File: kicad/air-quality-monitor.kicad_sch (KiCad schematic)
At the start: 28 parts, among them J1 USB-C power only, J2 SCD40 breakout, J3 OLED SSD1306, J4 SPS30, J5 Qwiic, J6 Qwiic, U1 AP2112K-3.3, U2 AP2112K-3.3, U3 ESP32-C6-DevKitC-1

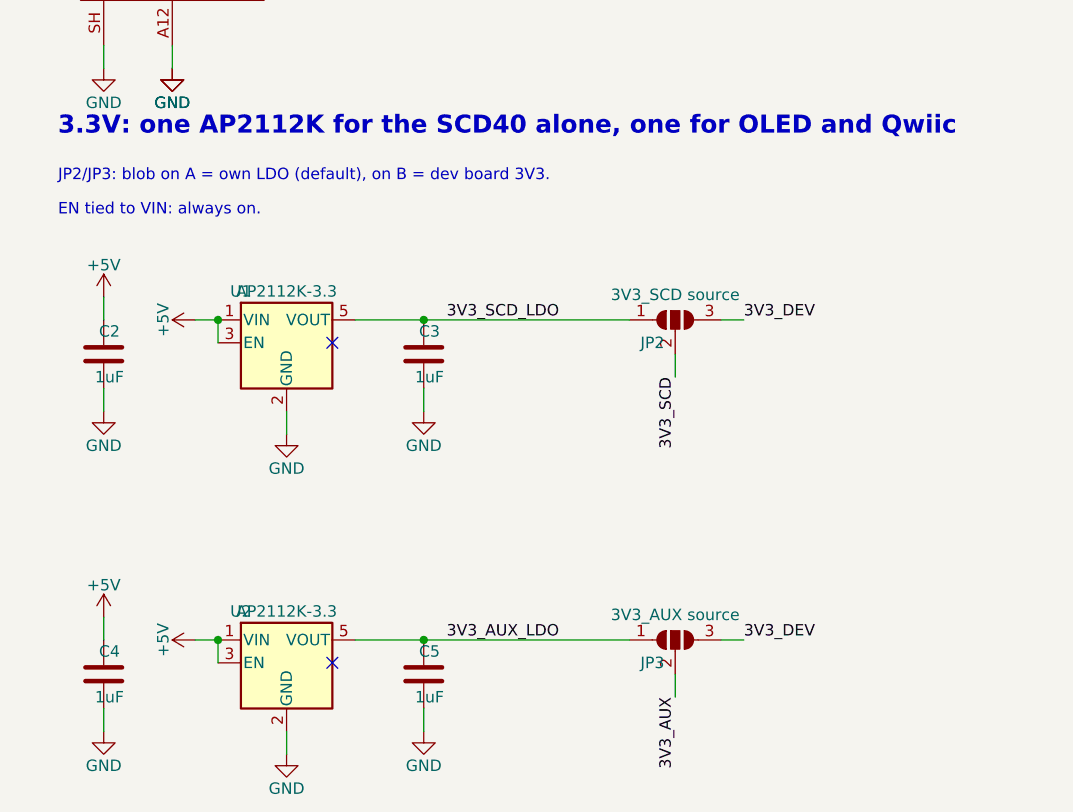
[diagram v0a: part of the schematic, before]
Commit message: Bridge both 3.3V jumpers to their LDO from the factory
With open jumpers the 3.3V rails were dead until a blob was soldered.
Now the board works as delivered, and switching a rail to the dev
board's 3V3 means cutting the trace and adding a blob.

Co-Authored-By: Claude Opus 5.5 <noreply@anthropic.com>
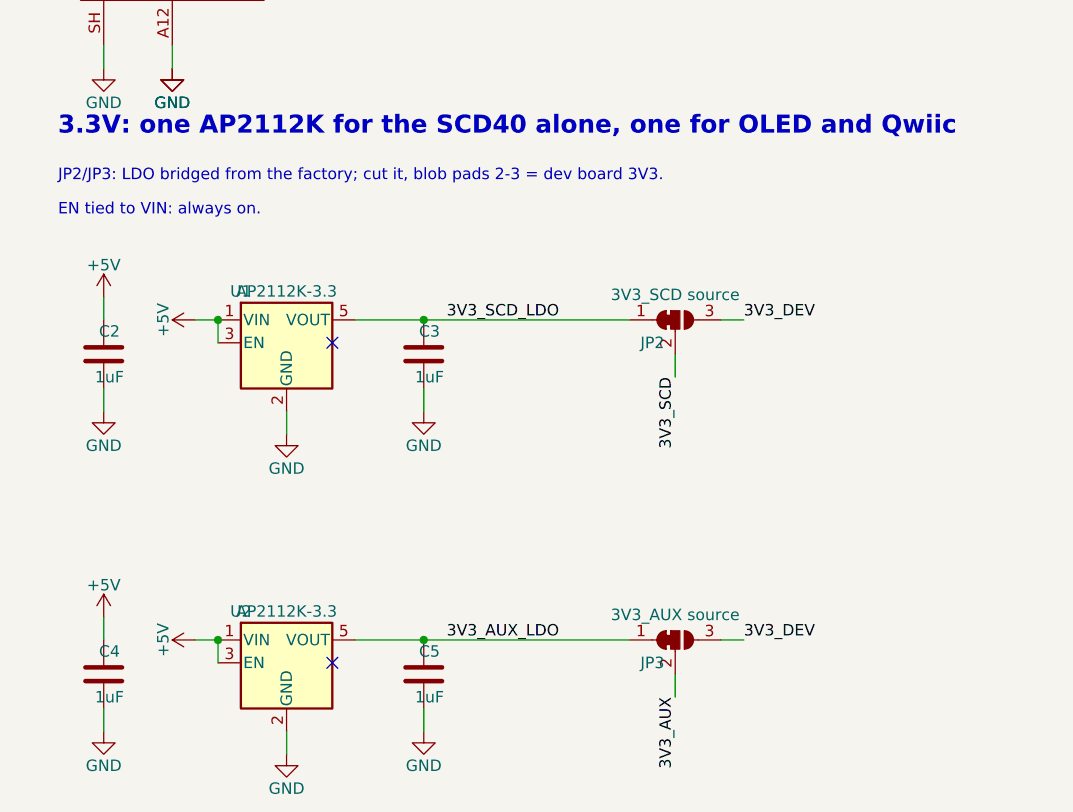
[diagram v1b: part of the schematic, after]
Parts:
- JP2, JP3: footprint Jumper:SolderJumper-3_P1.3mm_Open_RoundedPad1.0x1.5mm_NumberLabels -> Jumper:SolderJumper-3_P1.3mm_Bridged12_RoundedPad1.0x1.5mm_NumberLabels; symbol Jumper:SolderJumper_3_Open -> Jumper:SolderJumper_3_Bridged12
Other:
- note added: "JP2/JP3: LDO bridged from the factory; cut it, blob pads 2-3 = dev board 3V3."
- note removed: "JP2/JP3: blob on A = own LDO (default), on B = dev board 3V3."
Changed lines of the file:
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@@
 		)
 	)
-	(text "JP2/JP3: blob on A = own LDO (default), on B = dev board 3V3."
+	(text "JP2/JP3: LDO bridged from the factory; cut it, blob pads 2-3 = dev board 3V3."
 		(exclude_from_sim no)
 		(at 25.4 99.06 0)
@@
 	)
 	(symbol
-		(lib_id "Jumper:SolderJumper_3_Open")
+		(lib_id "Jumper:SolderJumper_3_Bridged12")
 		(at 93.98 149.86 0)
 		(unit 1)
@@
 			)
 		)
-		(property "Footprint" "Jumper:SolderJumper-3_P1.3mm_Open_RoundedPad1.0x1.5mm_NumberLabels"
+		(property "Footprint" "Jumper:SolderJumper-3_P1.3mm_Bridged12_RoundedPad1.0x1.5mm_NumberLabels"
 			(at 93.98 149.86 0)
 			(hide yes)
@@
 	)
 	(symbol
-		(lib_id "Jumper:SolderJumper_3_Open")
+		(lib_id "Jumper:SolderJumper_3_Bridged12")
 		(at 93.98 114.3 0)
 		(unit 1)
@@
 			)
 		)
-		(property "Footprint" "Jumper:SolderJumper-3_P1.3mm_Open_RoundedPad1.0x1.5mm_NumberLabels"
+		(property "Footprint" "Jumper:SolderJumper-3_P1.3mm_Bridged12_RoundedPad1.0x1.5mm_NumberLabels"
 			(at 93.98 114.3 0)
 			(hide yes)

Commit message: Use a jumper cap across D1 so the dev board gets the full 5V
Behind the Schottky the dev board's 5V pin sees about 4.6V, less than
the 4.9V that already sent an ESP32-S3 board with the same AMS1117
into a brownout loop. A cap fails safe: a loose one only puts the
diode back in the path. It comes off only when both USB cables are in.

Co-Authored-By: Claude Opus 5.5 <noreply@anthropic.com>
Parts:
- JP1: footprint Jumper:SolderJumper-2_P1.3mm_Open_RoundedPad1.0x1.5mm -> Connector_PinHeader_2.54mm:PinHeader_1x02_P2.54mm_Vertical; symbol Jumper:SolderJumper_2_Open -> Jumper:Jumper_2_Bridged
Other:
- note added: "JP1 cap on (default) bypasses D1: full 5V for the dev board. Pull it before plugging in both."
- note removed: "JP1 bridges the diode: dev board USB powers the PCB. Then never plug in both."
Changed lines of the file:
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@@
 		)
 	)
-	(text "JP1 bridges the diode: dev board USB powers the PCB. Then never plug in both."
+	(text "JP1 cap on (default) bypasses D1: full 5V for the dev board. Pull it before plugging in both."
 		(exclude_from_sim no)
 		(at 137.16 41.91 0)
@@
 	)
 	(symbol
-		(lib_id "Jumper:SolderJumper_2_Open")
+		(lib_id "Jumper:Jumper_2_Bridged")
 		(at 157.48 66.04 0)
 		(unit 1)
@@
 			)
 		)
-		(property "Footprint" "Jumper:SolderJumper-2_P1.3mm_Open_RoundedPad1.0x1.5mm"
+		(property "Footprint" "Connector_PinHeader_2.54mm:PinHeader_1x02_P2.54mm_Vertical"
 			(at 157.48 66.04 0)
 			(hide yes)

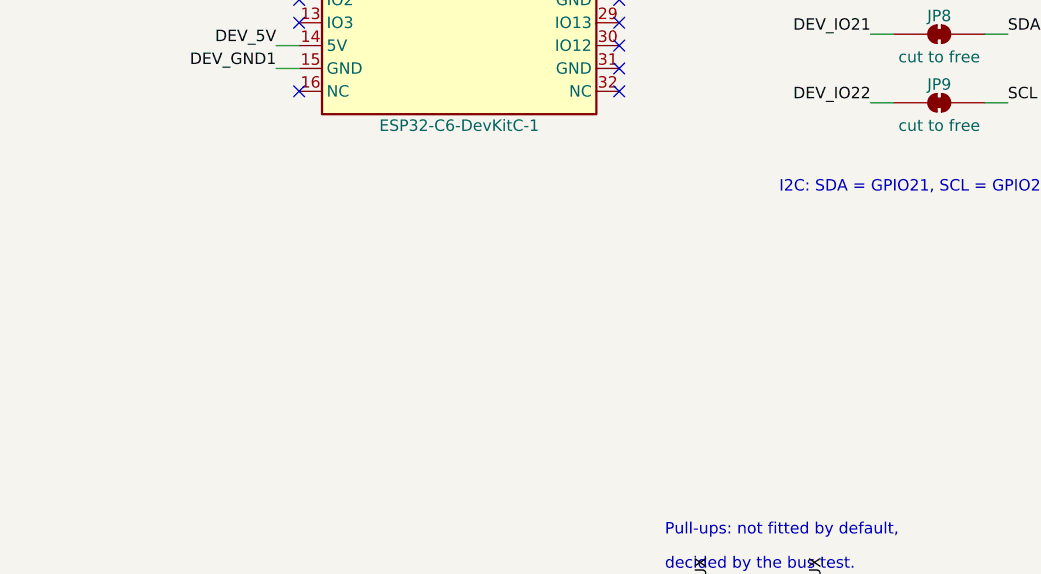
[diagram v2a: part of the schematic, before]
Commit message: Leave room for bulk capacitors on the dev board's 3V3
The same S3 board that browned out at 5.0V booted once 100+470µF sat
on its 3V3 pin. Two optional footprints there keep that fix one
solder job away, without fitting it on boards that don't need it.

Co-Authored-By: Claude Opus 5.5 <noreply@anthropic.com>
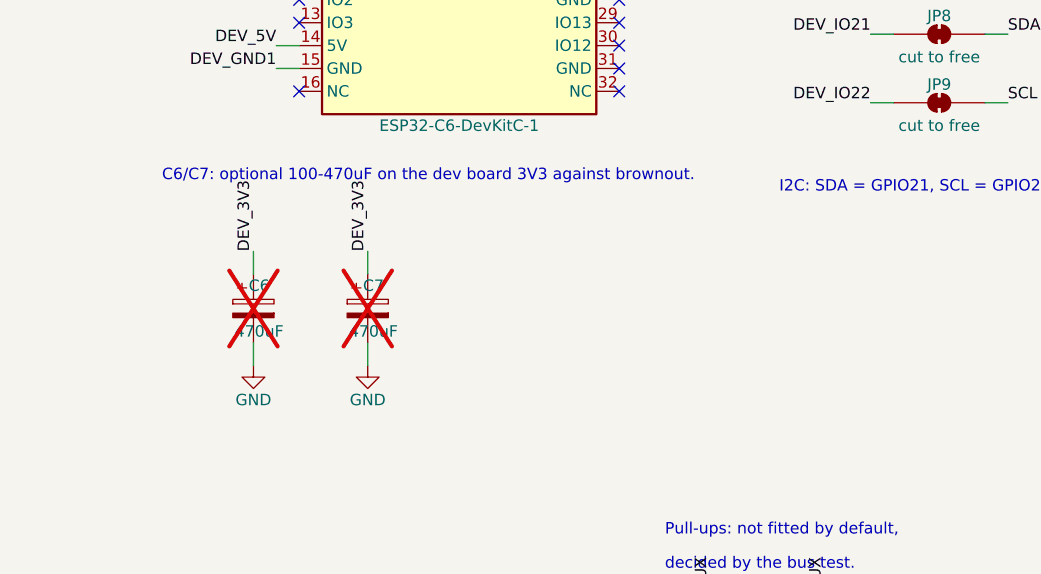
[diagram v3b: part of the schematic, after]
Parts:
- added C6, C7: 470uF, Capacitor_THT:CP_Radial_D8.0mm_P2.50mm, symbol Device:C_Polarized
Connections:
- net DEV_3V3: now also C6.1, C7.1
- net GND: now also C6.2, C7.2
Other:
- note added: "C6/C7: optional 100-470uF on the dev board 3V3 against brownout."

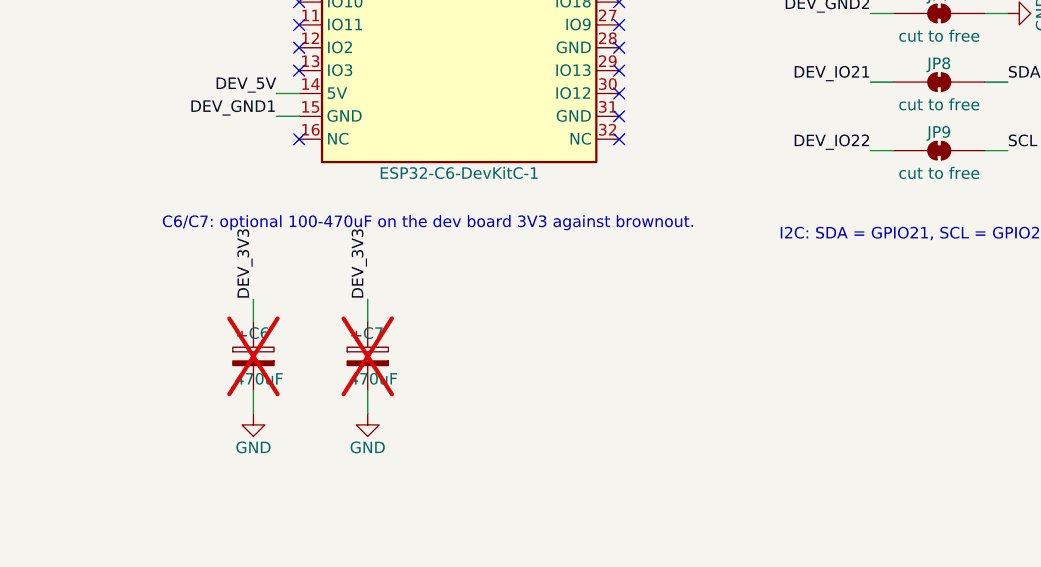
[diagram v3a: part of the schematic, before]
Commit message: Give the bulk capacitors the values that fixed the S3 board
"100-470uF" read as a range for both, while the fix on the S3 board
was one of each, 100uF plus 470uF.

Co-Authored-By: Claude Opus 5.5 <noreply@anthropic.com>
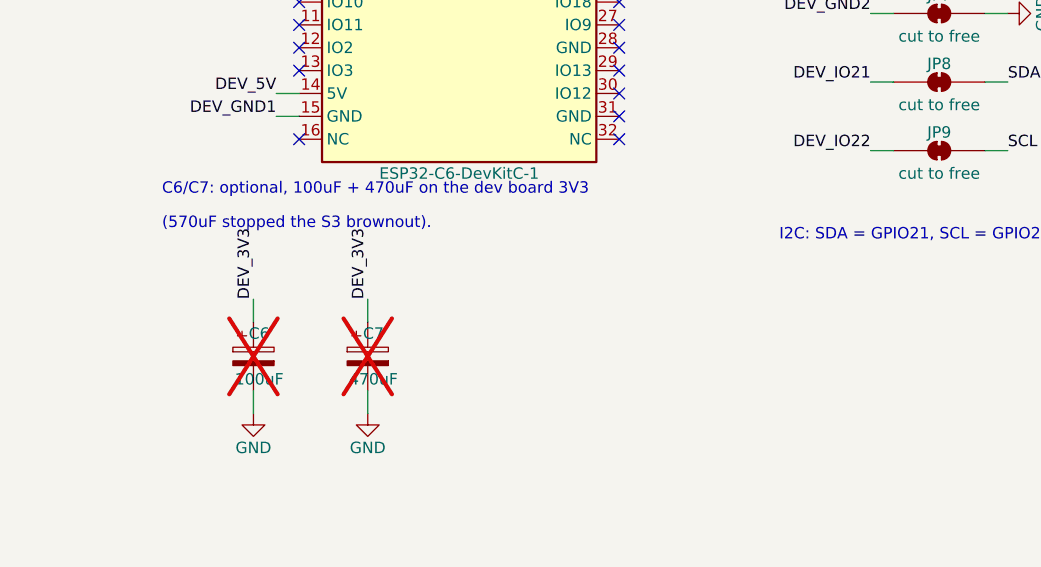
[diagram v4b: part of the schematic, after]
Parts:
- C6: value 470uF -> 100uF
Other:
- note added: "(570uF stopped the S3 brownout)."
- note added: "C6/C7: optional, 100uF + 470uF on the dev board 3V3"
- note removed: "C6/C7: optional 100-470uF on the dev board 3V3 against brownout."
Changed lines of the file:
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@@
 		)
 	)
-	(text "C6/C7: optional 100-470uF on the dev board 3V3 against brownout."
+	(text "C6/C7: optional, 100uF + 470uF on the dev board 3V3"
+		(exclude_from_sim no)
+		(at 167.64 157.48 0)
+		(effects
+			(font
+				(size 1.27 1.27)
+			)
+			(justify left bottom)
+		)
+	)
+	(text "(570uF stopped the S3 brownout)."
 		(exclude_from_sim no)
 		(at 167.64 161.29 0)
@@
 			)
 		)
-		(property "Value" "470uF"
+		(property "Value" "100uF"
 			(at 178.435 177.8 0)
 			(effects

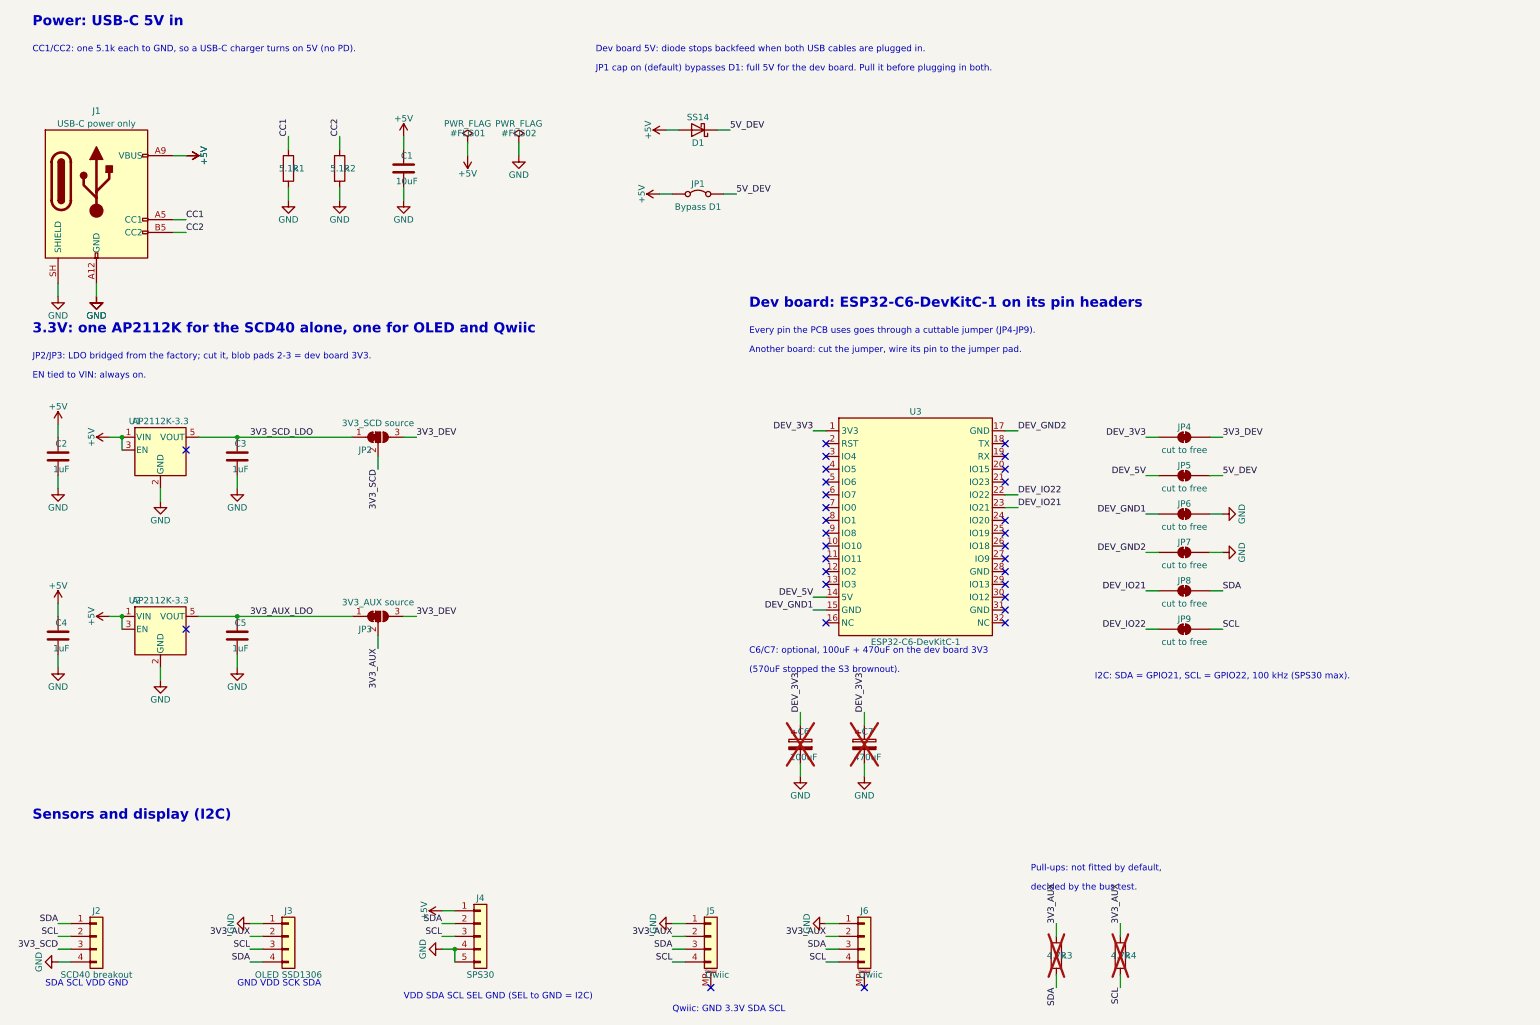
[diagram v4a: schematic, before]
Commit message: Let KiCad place the part labels
The generator put references and values on top of each other (U1 over
its value, the R and JP texts). KiCad's Autoplace Fields on the whole
sheet fixes most of them; saving also added KiCad's simulator defaults
to the project file.

Co-Authored-By: Claude Opus 5.5 <noreply@anthropic.com>
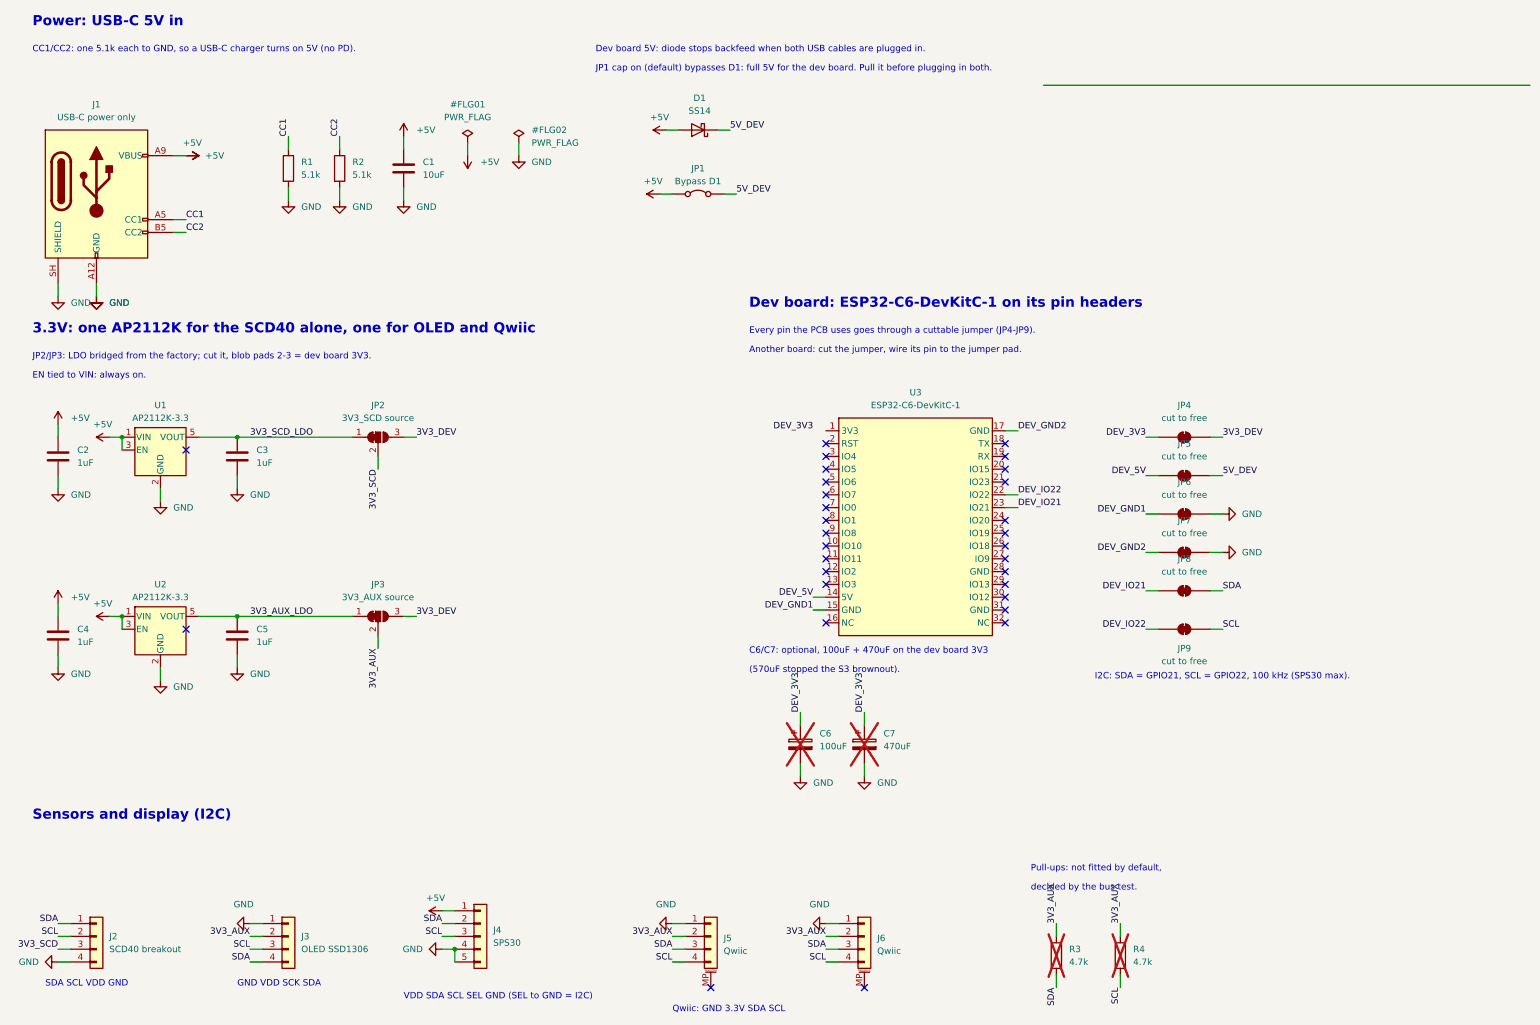
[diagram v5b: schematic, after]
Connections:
- net DEV_3V3: no longer U3.1 (3V3)

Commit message: Reconnect the dev board's 3V3 pin
The previous commit carried U3 pin 1's wire stub moved off to the top
of the sheet, so pin 1 was connected to nothing and DEV_3V3 dangled.
ERC flagged it; the wire is back where it was in ef42f9d.

Co-Authored-By: Claude Opus 5.5 <noreply@anthropic.com>
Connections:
- net DEV_3V3: now also U3.1 (3V3)
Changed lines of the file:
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@@
 	(wire
 		(pts
-			(xy 322.58 44.45) (xy 226.06 44.45)
+			(xy 182.88 113.03) (xy 180.34 113.03)
 		)
 		(stroke
